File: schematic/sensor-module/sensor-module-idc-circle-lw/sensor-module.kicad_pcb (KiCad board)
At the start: 2 copper layers, 29.5 x 29.5 mm, 15 parts, among them P1 SENSOR_CONNECTOR, P2 VibroEngine, U1 RGB-LED, U2 RGB-LED, U3 TSOP4856, U4 TSOP4856

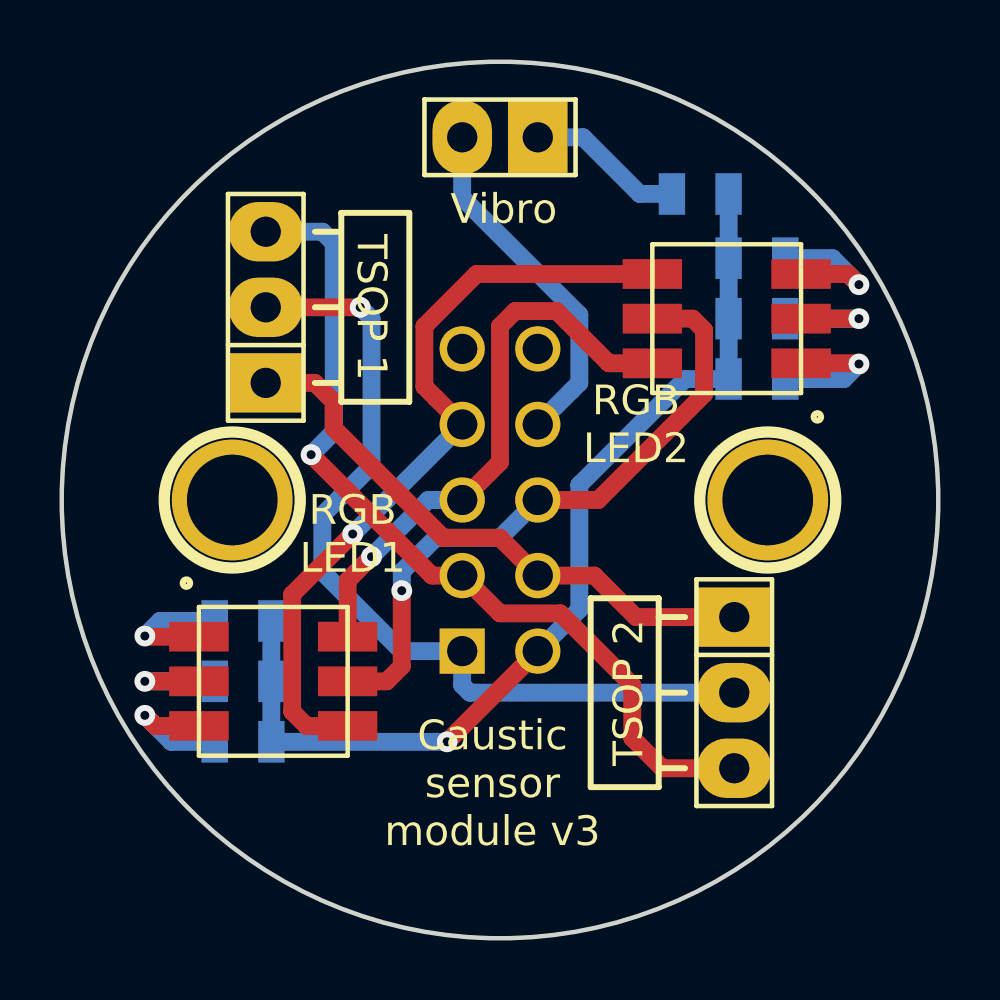
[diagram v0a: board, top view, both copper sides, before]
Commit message: Round sensor fix for TSOP orientation
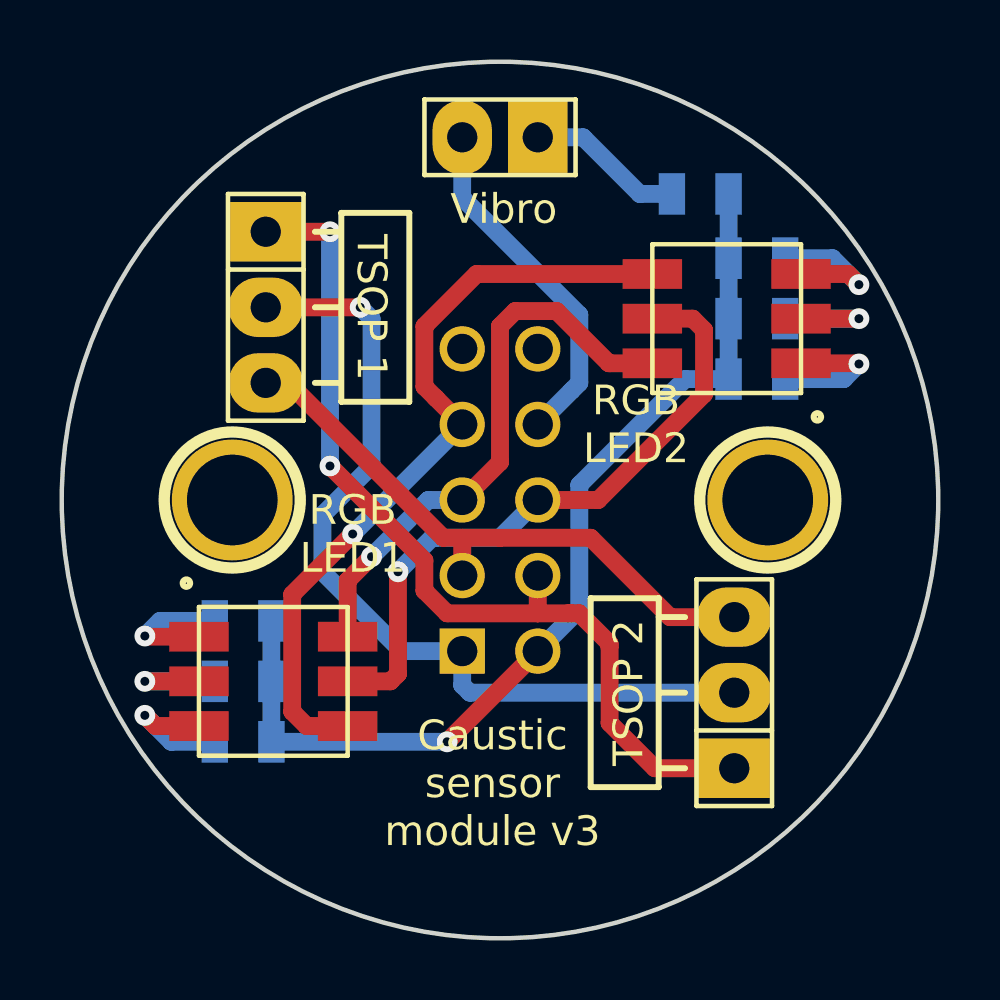
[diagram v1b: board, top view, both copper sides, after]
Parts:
- turned U3 to 90 degrees
- turned U4 to 270 degrees
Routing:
- net N-000003: track 19.5 -> 31.3 mm, vias 0 -> 2
- net +3.3V: track 29.5 -> 20.3 mm, vias 1 -> 0
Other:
- net class Default: clearance 0.2 -> 0.15
- rule trace_clearance: 0.2 -> 0.15
